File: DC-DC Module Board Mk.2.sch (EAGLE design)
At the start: 23 parts, among them Q1 SUM90P10-19L

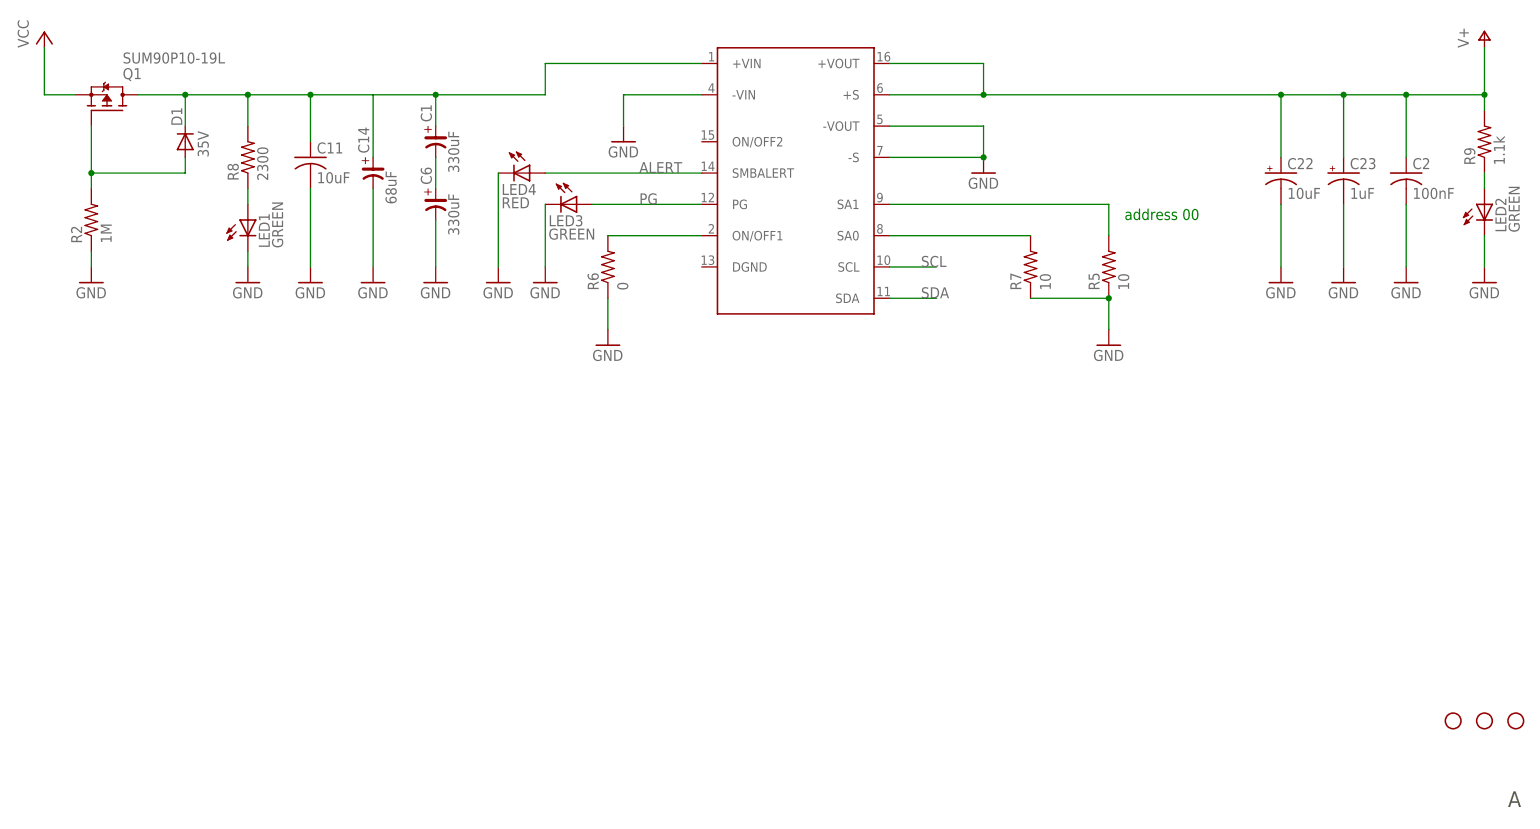
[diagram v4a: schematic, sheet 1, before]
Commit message: got rid of old capacitors and added connectors
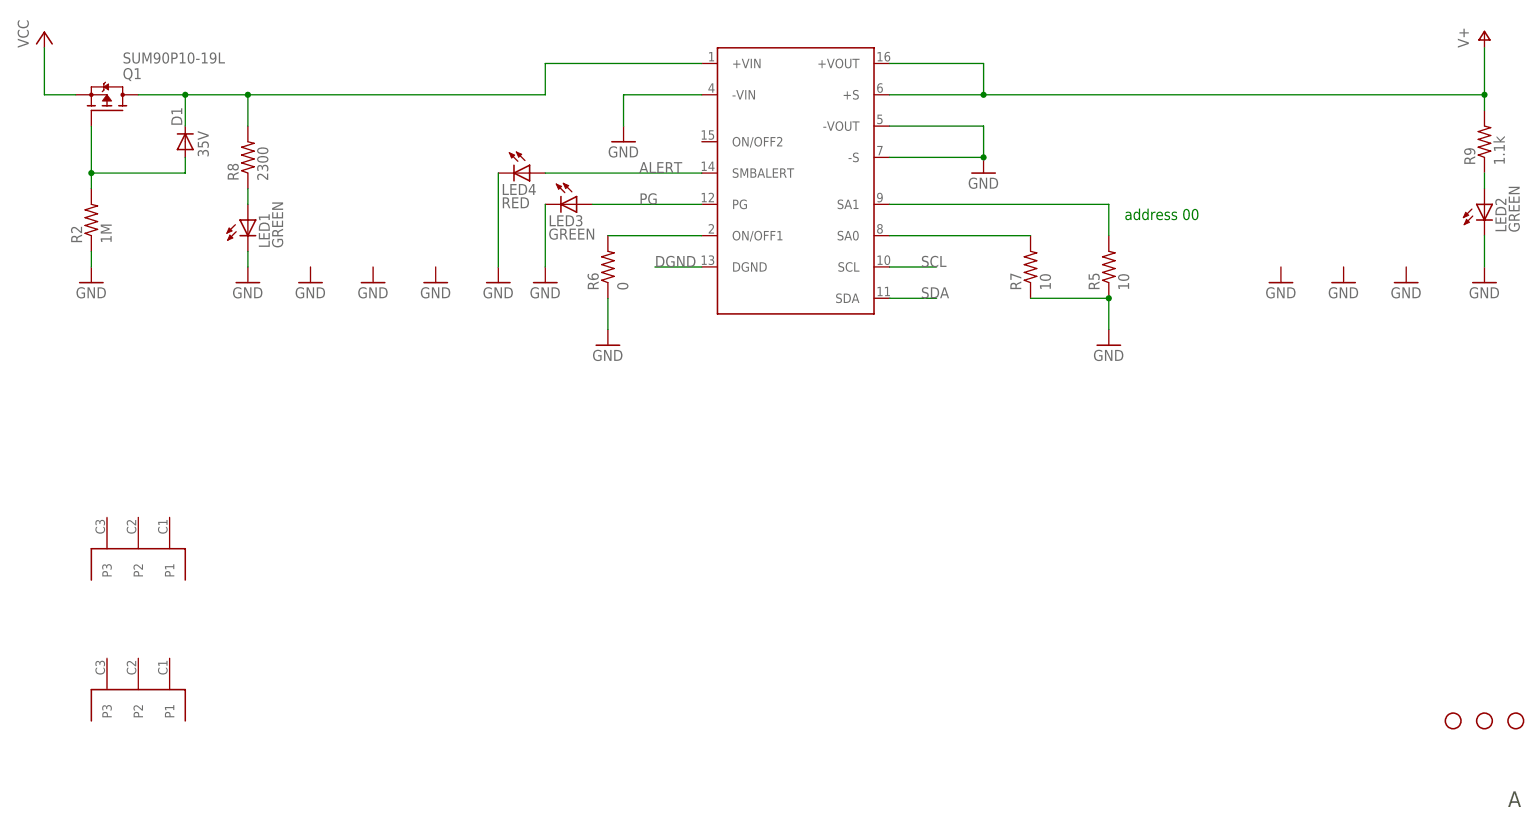
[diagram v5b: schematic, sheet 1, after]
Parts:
- removed C1, C6: 330uF, rc-master:CP_SV-H
- removed C11: 10uF, resistor:C-USC2220K
- removed C14: 68uF, rc-master:CP_SV-H
- removed C2: 100nF, resistor:C-USC0603
- removed C22: 10uF, SparkFun:CAP_POL7343
- removed C23: 1uF, SparkFun:CAP_POL3528
- added U$2, U$3: MICRO-FIT-3-SMD, Connectors:MICRO-FIT-3-SMD
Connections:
- removed net N$4: C1.-, C6.+
- new net DGND: U$1.DGND
- net GND: no longer C11.2, C14.-, C2.2, C22.-, C23.-, C6.-
- net N$6: no longer C1.+, C11.1, C14.+
- net V+: no longer C2.1, C22.+, C23.+

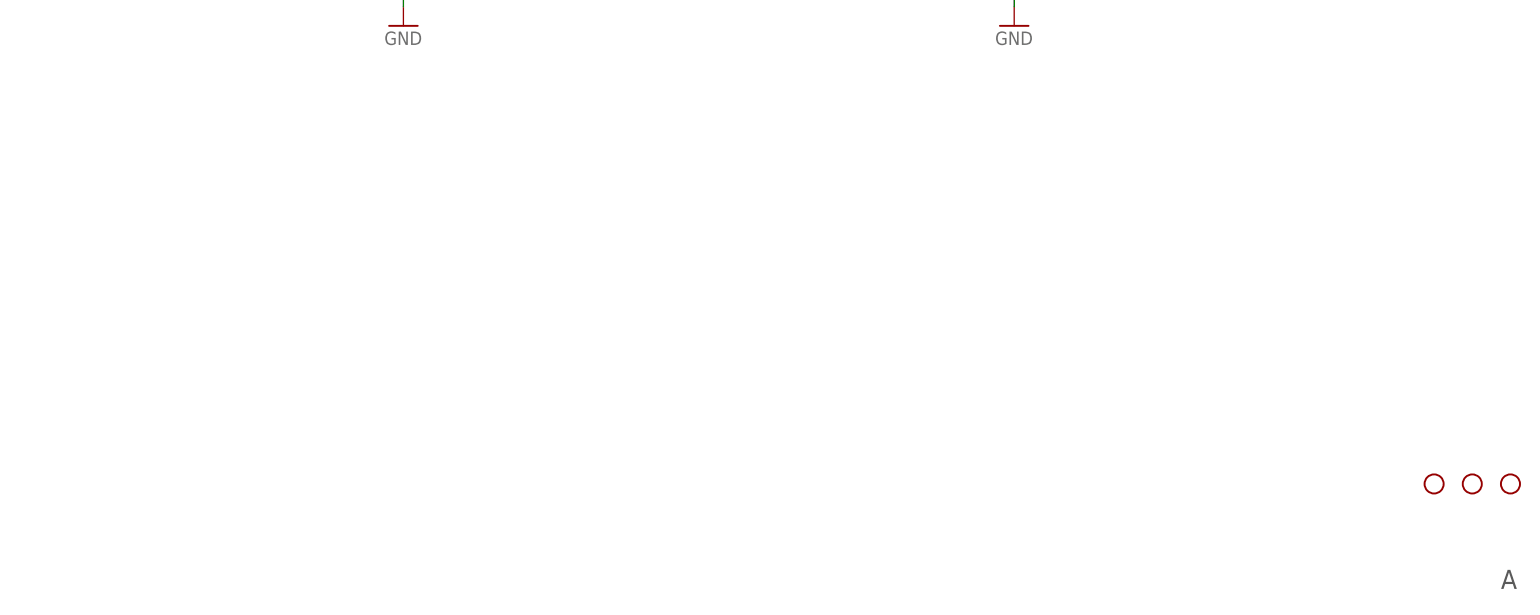
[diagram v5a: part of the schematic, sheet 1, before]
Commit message: added 48V connector
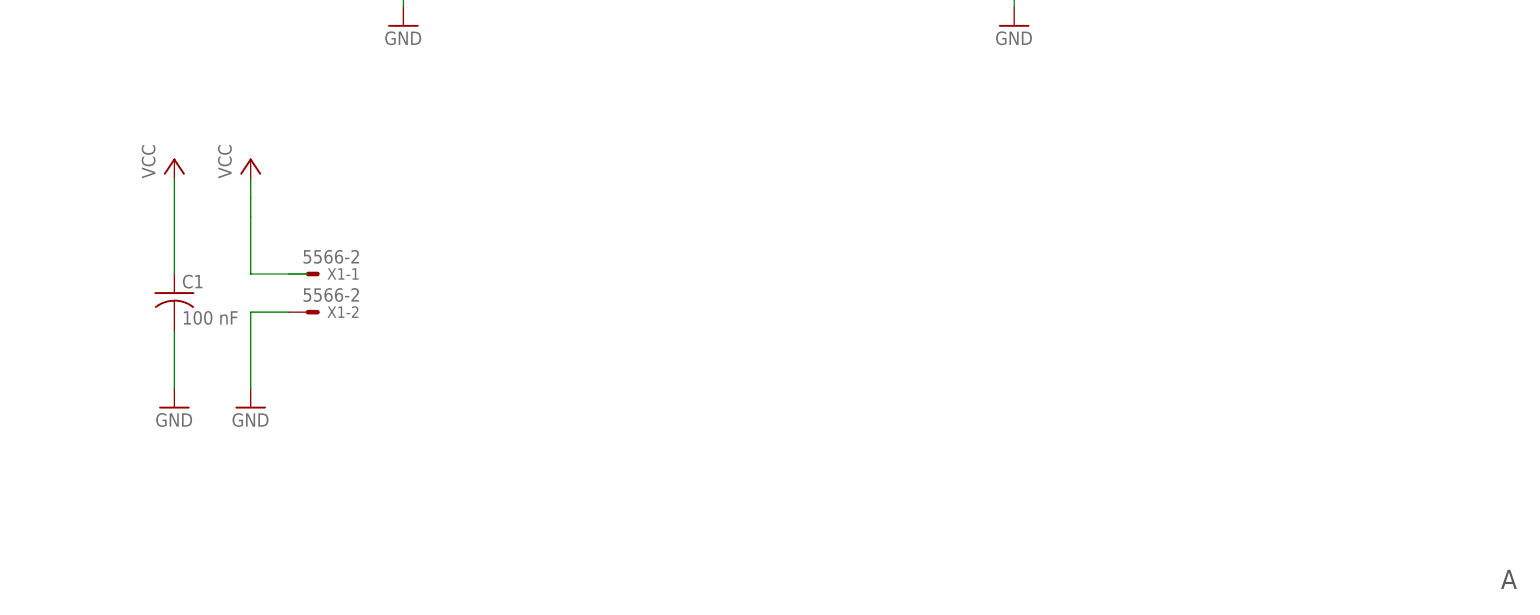
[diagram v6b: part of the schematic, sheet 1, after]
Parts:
- removed JP1, JP2, JP4: STAND-OFF, SparkFun:STAND-OFF
- added C1: 100 nF, resistor:C-USC0603
- added X1: 5566-2, con-molex:5566-2
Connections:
- net GND: now also C1.2, X1-2.S
- net VCC: now also C1.1
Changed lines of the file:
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@@
 </classes>
 <parts>
-<part name="JP1" library="SparkFun" deviceset="STAND-OFF" device=""/>
-<part name="JP2" library="SparkFun" deviceset="STAND-OFF" device=""/>
-<part name="JP4" library="SparkFun" deviceset="STAND-OFF" device=""/>
 <part name="GND3" library="supply1" deviceset="GND" device=""/>
 <part name="GND4" library="supply1" deviceset="GND" device=""/>
@@
 <part name="U$2" library="Connectors" deviceset="MICRO-FIT-3-SMD" device=""/>
 <part name="U$3" library="Connectors" deviceset="MICRO-FIT-3-SMD" device=""/>
+<part name="X1" library="con-molex" deviceset="5566-2" device=""/>
+<part name="P+1" library="supply1" deviceset="VCC" device=""/>
+<part name="GND14" library="supply1" deviceset="GND" device=""/>
+<part name="C1" library="resistor" deviceset="C-US" device="C0603" value="100 nF"/>
+<part name="P+2" library="supply1" deviceset="VCC" device=""/>
+<part name="GND15" library="supply1" deviceset="GND" device=""/>
 </parts>
 <sheets>
@@
 </plain>
 <instances>
-<instance part="JP1" gate="G$1" x="246.38" y="25.4"/>
-<instance part="JP2" gate="G$1" x="241.3" y="25.4"/>
-<instance part="JP4" gate="G$1" x="236.22" y="25.4"/>
 <instance part="GND3" gate="1" x="208.28" y="96.52"/>
 <instance part="GND4" gate="1" x="218.44" y="96.52"/>
@@
 <instance part="U$2" gate="G$1" x="22.86" y="50.8"/>
 <instance part="U$3" gate="G$1" x="22.86" y="27.94"/>
+<instance part="X1" gate="-1" x="86.36" y="53.34"/>
+<instance part="X1" gate="-2" x="86.36" y="48.26"/>
+<instance part="P+1" gate="VCC" x="78.74" y="68.58"/>
+<instance part="GND14" gate="1" x="78.74" y="35.56"/>
+<instance part="C1" gate="G$1" x="68.58" y="50.8"/>
+<instance part="P+2" gate="VCC" x="68.58" y="68.58"/>
+<instance part="GND15" gate="1" x="68.58" y="35.56"/>
 </instances>
 <busses>
@@
 <wire x1="114.3" y1="127" x2="101.6" y2="127" width="0.1524" layer="91"/>
 <wire x1="101.6" y1="127" x2="101.6" y2="121.92" width="0.1524" layer="91"/>
+</segment>
+<segment>
+<pinref part="X1" gate="-2" pin="S"/>
+<wire x1="83.82" y1="48.26" x2="78.74" y2="48.26" width="0.1524" layer="91"/>
+<pinref part="GND14" gate="1" pin="GND"/>
+<wire x1="78.74" y1="48.26" x2="78.74" y2="38.1" width="0.1524" layer="91"/>
+</segment>
+<segment>
+<pinref part="C1" gate="G$1" pin="2"/>
+<pinref part="GND15" gate="1" pin="GND"/>
+<wire x1="68.58" y1="45.72" x2="68.58" y2="38.1" width="0.1524" layer="91"/>
 </segment>
 </net>
@@
 <pinref part="Q1" gate="G$1" pin="S"/>
 </segment>
-</net>
+<segment>
+<wire x1="86.36" y1="53.34" x2="78.74" y2="53.34" width="0.1524" layer="91"/>
+<wire x1="78.74" y1="53.34" x2="78.74" y2="60.96" width="0.1524" layer="91"/>
+<pinref part="P+1" gate="VCC" pin="VCC"/>
+<wire x1="78.74" y1="60.96" x2="78.74" y2="63.5" width="0.1524" layer="91"/>
+<wire x1="78.74" y1="66.04" x2="78.74" y2="63.5" width="0.1524" layer="91"/>
+</segment>
+<segment>
+<pinref part="P+2" gate="VCC" pin="VCC"/>
+<pinref part="C1" gate="G$1" pin="1"/>
+<wire x1="68.58" y1="66.04" x2="68.58" y2="53.34" width="0.1524" layer="91"/>
+</segment>
+</net>

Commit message: four pin connectors
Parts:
- removed U$2, U$3: MICRO-FIT-3-SMD, Connectors:MICRO-FIT-3-SMD
- removed X1: 5566-2, con-molex:5566-2
- added ASV: 8.000MHZ, DiscreteComponents:ASF
- added BSS138: n-chanel mosfet, DiscreteComponents:BSS138
- added C10, C12, C13, C4, C5, C6, C7: 0.1uF, rcl:C-USC0603
- added C11: 1uF, rcl:C-USC0603
- added C14, C15, C16: .1u, rcl:C-USC0603
- added C19, C20: 15u, rcl:C-USC3216
- added C2, C3: 2.2uF, rcl:C-USC0603
- added C21: 10u, rcl:C-USC0603
- added C8: 10nF, rcl:C-USC0603
- added C9: 4.7uF, rcl:C-USC0603
- added D2: (no value), DiscreteComponents:DIODE-DO-214AC
- added D3: Yellow, SparkFun-LED:LED-YELLOW0603
- added D4: RED, SparkFun-LED:LED-RED0603
- added D5: BLUE, SparkFun-LED:LED-BLUE0603
- added D6: GREEN, SparkFun-LED:LED-GREEN0603
- added R1, R10, R11, R12, R13, R14, R15, R16, R3, R4: 10K, rcl:R-US_R0603
- added R17: 120, rcl:R-US_R0603
- added R18: 100K, rcl:R-US_R0603
- added R19, R20: 0, resistor:R-US_R0603
- added RN1: (no value), DiscreteComponents:2R-NEXBV4V
- added T1: FDN340P, DiscreteComponents:FDN340P
- added U$10, U$11: MICRO-FIT-4-SMD-PART, Connectors:MICRO-FIT-4-SMD-PART
- added U$4, U$6: SWITCH, DiscreteComponents:SWITCH
- added U$5: STM32F405, Other:STM32F405
- added U$7: MICROUSB, Other:MICROUSB
- added U$8: MAX3051MAX3051, MAX3051 Library:MAX3051MAX3051
- added U$9: BSS138, DiscreteComponents:BSS138
- added X2: 5566-2, con-molex:5566-2
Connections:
- removed net N$6: D1.C, Q1.D, R8.2, U$1.+VIN
- new net +3V3: ASV.VCC, BSS138.G, C10.1, C11.1, C13.1, C4.1, C5.1, C6.1, C7.1, C8.1, C9.1, R15.2, R16.2, R3.2, U$4.P$2, U$5G$4.VBAT, U$5G$4.VDD, U$5G$4.VDDA, U$8.VCC, U$9.G
- new net +5V: D2.A, R13.2, R14.2, T1.G
- new net BOOT0: R1.2, U$4.P$1, U$5G$5.BOOT0
- new net CANH: R17.1, U$8.CANH
- new net CANL: R17.2, U$8.CANL
- new net N$2: C14.1, C15.1, C16.1, D1.C, Q1.D, R8.2, U$1.+VIN
- new net N$24: RN1B.1, U$7.D+
- new net N$3: LED4.C, R19.2
- new net N$4: LED3.C, R20.2
- new net N$56: RN1A.1, U$7.D-
- new net N$57: T1.D, U$7.VCC
- new net N$58: D2.C, T1.S
- new net N$59: D3.A, R4.1
- new net N$60: D4.A, R10.1
- new net N$61: D5.A, R11.1
- new net N$62: D6.A, R12.1
- new net N$63: R18.1, U$8.RS
- new net NRST: C12.1, R3.1, U$5G$6.NRST, U$6.P$1
- new net OSCIN: ASV.FO, U$5G$7.PH0_OSCIN
- new net OSCOUT: U$5G$7.PH1_OSCOUT
- new net PIN10: U$5G$3.PC2
- new net PIN11: U$5G$3.PC3
- new net PIN14: U$5G$1.PA0_WKUP
- new net PIN15: U$5G$1.PA1
- new net PIN16: U$5G$1.PA2
- new net PIN17: U$5G$1.PA3
- new net PIN2: U$5G$3.PC13
- new net PIN20: U$5G$1.PA4
- new net PIN21: U$5G$1.PA5
- new net PIN22: U$5G$1.PA6
- new net PIN23: U$5G$1.PA7
- new net PIN24: U$5G$3.PC4
- new net PIN25: U$5G$3.PC5
- new net PIN26: U$5G$2.PB0
- new net PIN27: U$5G$2.PB1
- new net PIN29: U$5G$2.PB10
- new net PIN3: U$5G$3.PC14
- new net PIN30: U$5G$2.PB11
- new net PIN33: U$5G$2.PB12
- new net PIN34: U$5G$2.PB13
- new net PIN35: U$5G$2.PB14
- new net PIN36: U$5G$2.PB15
- new net PIN37: U$5G$3.PC6
- new net PIN38: U$5G$3.PC7
- new net PIN39: U$5G$3.PC8
- new net PIN4: U$5G$3.PC15
- new net PIN40: U$5G$3.PC9
- new net PIN41: U$5G$1.PA8
- new net PIN42: U$5G$1.PA9
- new net PIN43: U$5G$1.PA10
- new net PIN44: RN1A.2, U$5G$1.PA11
- new net PIN45: RN1B.2, U$5G$1.PA12
- new net PIN46: U$5G$1.PA13
- new net PIN49: U$5G$1.PA14
- new net PIN50: U$5G$1.PA15
- new net PIN51: U$5G$3.PC10
- new net PIN52: U$5G$3.PC11
- new net PIN53: U$5G$3.PC12
- new net PIN54: U$5G$8.PD2
- new net PIN55: U$5G$2.PB3
- new net PIN56: U$5G$2.PB4
- new net PIN57: U$5G$2.PB5
- new net PIN58: U$5G$2.PB6
- new net PIN59: U$5G$2.PB7
- new net PIN61: U$5G$2.PB8
- new net PIN62: U$5G$2.PB9
- new net PIN8: U$5G$3.PC0
- new net PIN9: U$5G$3.PC1
- new net RXD: U$8.RXD
- new net SCL1: BSS138.S, R15.1
- new net SCL2: BSS138.D, R13.1
- new net SDA1: R16.1, U$9.S
- new net SDA2: R14.1, U$9.D
- new net TXD: U$8.TXD
- new net VCAP_1: C2.1, U$5G$4.VCAP_1
- new net VCAP_2: C3.1, U$5G$4.VCAP_2
- net GND: now also ASV.GND, C10.2, C11.2, C12.2, C13.2, C14.2, C15.2, C16.2, C19.2, C2.2, C20.2, C21.2, C3.2, C4.2, C5.2, C6.2, C7.2, C8.2, C9.2, D3.C, D4.C, D5.C, D6.C, R1.1, R18.2, R19.1, R20.1, U$5G$2.PB2, U$5G$4.VSS, U$5G$4.VSSA, U$6.P$2, U$7.GND, U$7.ID, U$8.GND, X2-1.S; no longer LED3.C, LED4.C, X1-2.S
- net V+: now also C19.1, C20.1, C21.1
- net VCC: now also X2-2.S
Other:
- note added: ": pins 18, 63"
- note added: ": pins 19, 32, 48, 64"
- note added: "Between VDDA and VSSA"
- note added: "Bi-Directional Level Shifter"
- note added: "Conect to any one VDD"
- note added: "Micro USB"
- note added: "Missing AP1117... Regulator"
- note added: "One for each VDD"
- note added: "Yes we CAN!"

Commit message: power connectors, board layout basic
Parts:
- added C17, C18: 1uF, SparkFun-Passives:CAP0603-CAP
- added C22, C24: 10uF, ux-capacitor:NICHICON-UX-8X10
- added C23: 22uF, ux-capacitor:NICHICON-UX-8X10
- added U$12: NCP1117, PowerComponents:NCP1117
- added U$2, U$3: XT60, Connectors:XT60
- R19, R20: value 0 -> 1k
- R5, R7: value 10 -> 10k
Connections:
- removed net PIN58: U$5G$2.PB6
- removed net PIN59: U$5G$2.PB7
- removed net V+: C19.1, C20.1, C21.1, R9.2, U$1.+S, U$1.+VOUT
- new net +12V1: C19.1, C20.1, C21.1, R9.2, U$1.+S, U$1.+VOUT, U$2.+12V, U$3.+12V
- new net +12V5: C17.1, U$12.INPUT
- net +3V3: now also C18.1, U$12.OUTPUT, U$12.TABOUT
- net GND: now also C17.2, C18.2, C22.P$2, C23.P$2, C24.P$2, U$12.GND
- net N$2: now also C22.P$1, C23.P$1, C24.P$1
- net SCL: now also U$5G$2.PB6
- net SDA: now also U$5G$2.PB7
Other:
- note added: "3.3V Linear Regulator"
- note added: "48V connector"
- note added: "Brick 1"
- note added: "address 04"
- note removed: "address 00"
- moved on the sheet: C1, U$10, U$11, X2-1, X2-2
